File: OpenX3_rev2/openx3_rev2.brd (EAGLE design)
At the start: 47 x 49.5 mm, 34 parts, among them IC1 24AA256SN, J1 BM20B-SRDS-G-TF(LF)(SN), J2 SM12B-SRSS-TB(LF)(SN), J3 53398-0271, J4 1734260-3, U1 LC4256V-75TN100CTQFP100-L, U2 AM29F016D-70EF, U3 AM29F002BB90EI

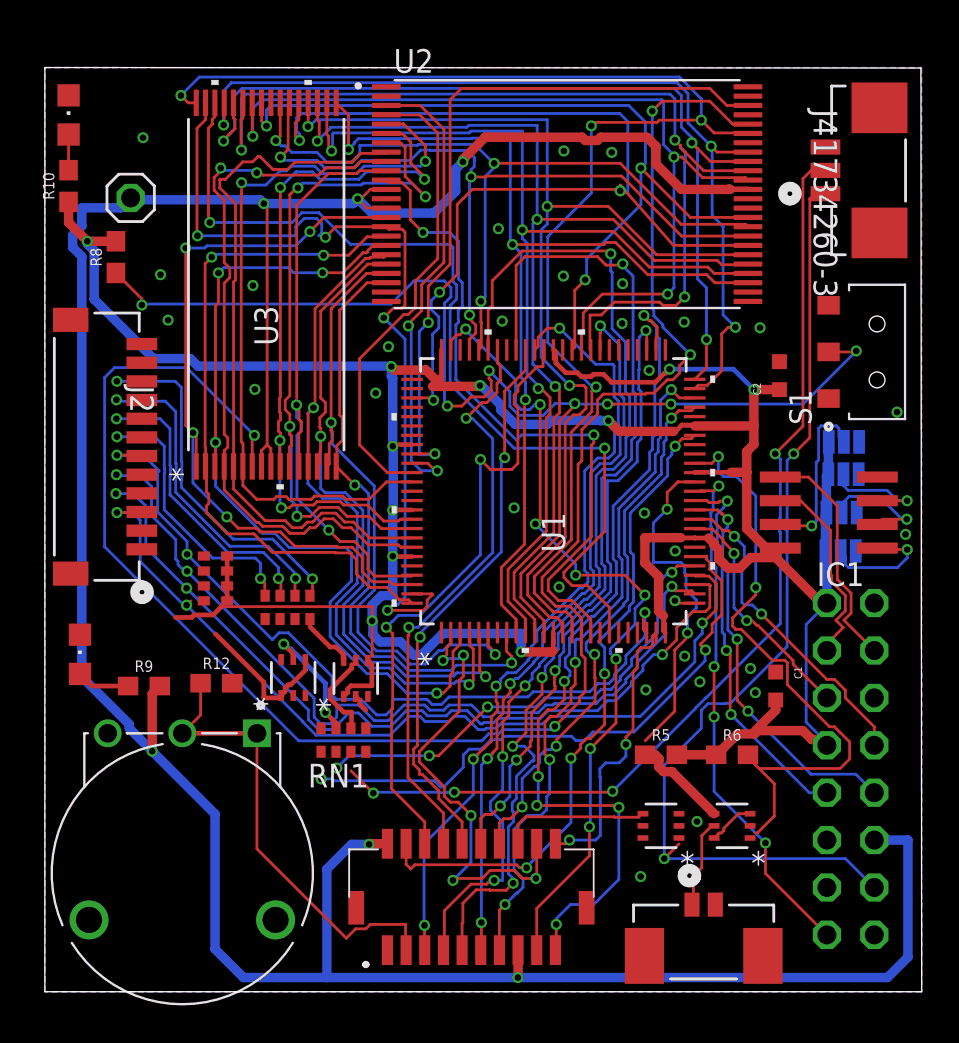
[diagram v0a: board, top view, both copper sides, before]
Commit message: minor fixes to traces, but no changes, adding gerber file for 2nd pcb order with fixed 3v3 and gnd
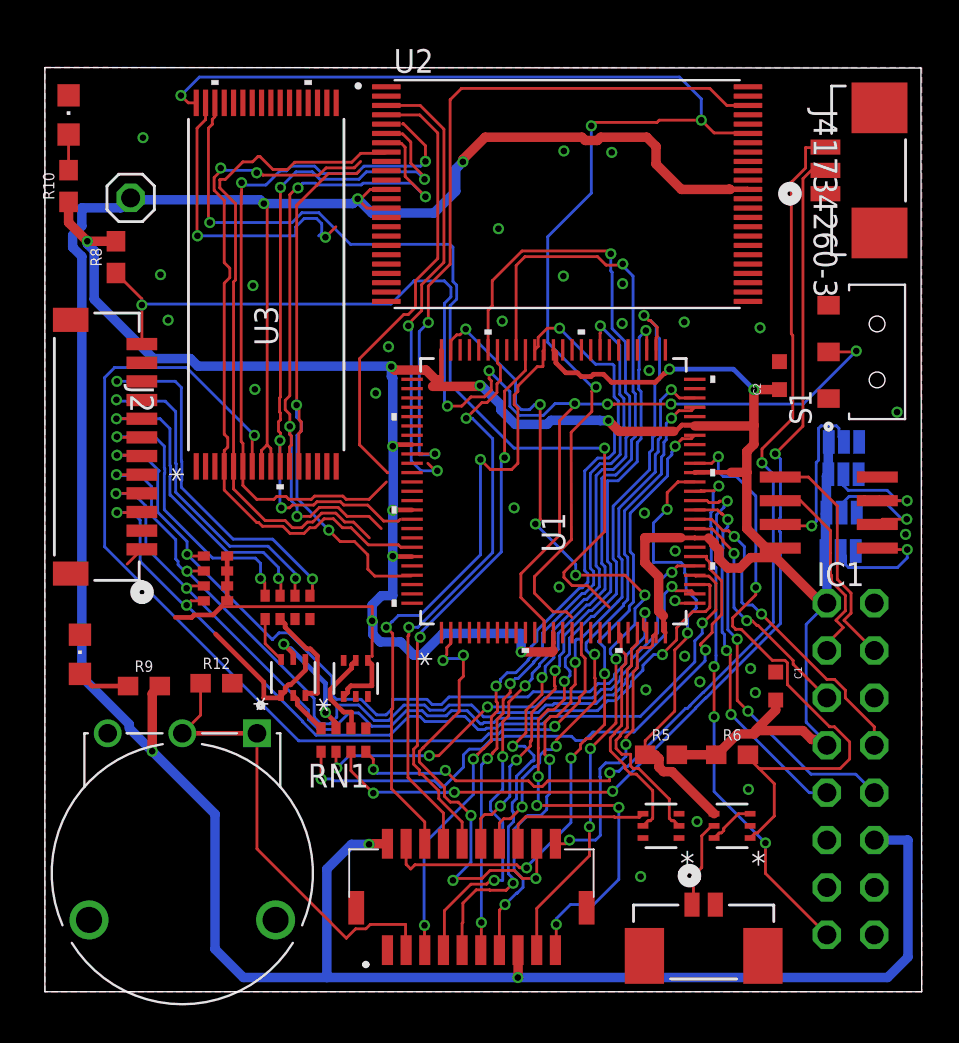
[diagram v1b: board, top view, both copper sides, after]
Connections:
- net BLUELEDACT renamed N$6
- net BLUELED_O renamed N$74
- net D0_O renamed D0
- net LANACT_O renamed LANLED_O
- net REDLEDACT renamed N$71
- net REDLED_O renamed N$75
- removed net BLUELED_I: RN1.2
- removed net DO_CTRL: R2.5
- removed net FPEJECT: R1.1, R6.2
- removed net FPPWR: R1.4, R5.1
- removed net HDDACT_0: R3.3
- removed net HDDACT_O: RN3.3
- removed net K_PWM: R2.2
- removed net N$56: R1.3, R1.6
- removed net REDLED_I: RN1.1
- removed net SWBABK3: RN2.7
- new net HDDLED_O: R3.3, RN3.3
- new net N$62: R2.2, U1.22
- new net N$63: R2.5, U1.20
- net A4: no longer U3.16
- net A5: no longer U3.15
- net A7: now also U3.15
- net A8: now also U3.16
- net GND: now also R1.3, R1.6
- net N$59: now also R1.4, R5.1
- net N$61: now also R1.1, R6.2
- net N$78: now also RN1.1
- net N$79: now also RN1.2
- net SWBANK3: now also RN2.7
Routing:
- net A0: track 57.6 -> 0.00 mm, vias 3 -> 0
- net A1: track 56.3 -> 0.00 mm, vias 3 -> 0
- net DQ0: track 56.1 -> 0.00 mm, vias 4 -> 0
- net A2: track 55.8 -> 0.00 mm, vias 3 -> 0
- net LANACT_I: track 0.00 -> 54.7 mm, vias 0 -> 4
- net A3: track 53.0 -> 0.00 mm, vias 3 -> 0
- net D0: track 52.8 -> 0.00 mm, vias 2 -> 0
- net DQ5: track 51.8 -> 0.00 mm, vias 3 -> 0
- net DQ6: track 48.8 -> 0.00 mm, vias 3 -> 0
- net DQ7: track 48.7 -> 0.00 mm, vias 3 -> 0
- net DQ4: track 47.7 -> 0.00 mm, vias 3 -> 0
- net A8: track 47.3 -> 0.00 mm, vias 4 -> 0
- net DQ3: track 43.7 -> 0.00 mm, vias 3 -> 0
- net DQ1: track 41.2 -> 0.00 mm, vias 3 -> 0
- net WE#: track 96.1 -> 55.1 mm, vias 4 -> 2
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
